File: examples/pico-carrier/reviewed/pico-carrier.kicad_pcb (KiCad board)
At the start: 2 copper layers, 88 x 62 mm, 16 parts, among them J1 5V IN, J3 GP0-GP15, J4 GP16-GP28, PWR, U1 Pico

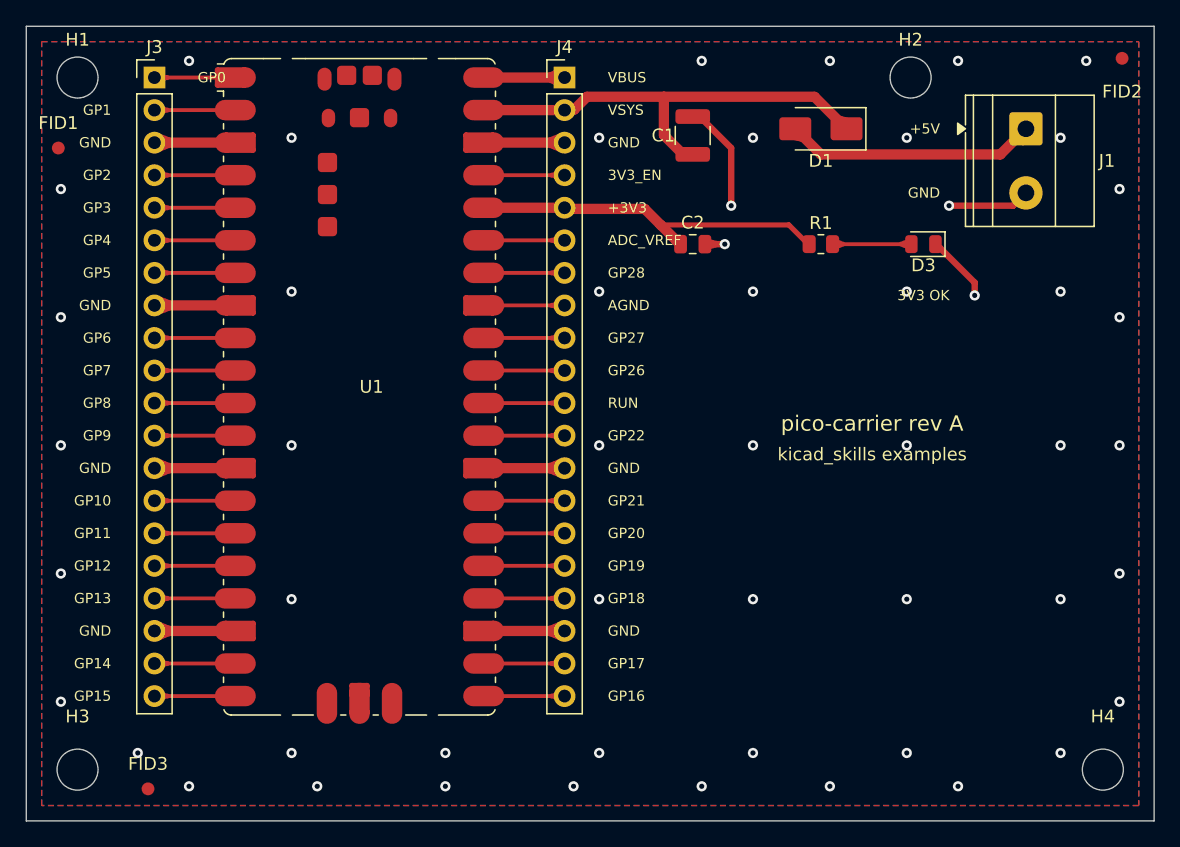
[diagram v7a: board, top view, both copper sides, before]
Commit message: Leave room for the screw, and print the ink where the board is
The screw holes were placed against the hole's own courtyard, which is the
drill plus a whisker - so on four of the five boards a hole sat inside a
connector's mating space, closest 0.42 mm. What goes through an M3 hole is a
pan head on a washer, seven millimetres of steel lying flat, and a connector
wants its shell, its wires and the fingers that fit them on top of that. The
spot search now keeps the fastener's own circle clear of every part body and
gives connectors CONNECTOR_ACCESS more, and three rules say so when a board
does not: mechanical.fastener_clearance, mechanical.connector_access and
mechanical.fastener_copper, all blocking for a generated design.

Silk was measured with a per-character advance of 0.78, and KiCad's stroke
font is proportional at 0.94 to 1.07. Everything downstream of that estimate
was placing ink where it did not fit: a legend across a capacitor's land, a
designator through the board's own name. `_text_extent` takes the top of the
measured range, adds the fab's clearance and is used by every silk placement.

Three placements also fell through to a position nobody chose. A designator
that found nothing kept its library offset, which for a part in a corner
points off the board; the board id took the first of eight fixed strips; a
legend took the least bad of six spots. All three are scored now, over
candidate sets wide enough to have an answer - and a pad-less footprint, which
is what a mounting hole is, is no longer skipped outright.

silk.off_board reports the case KiCad's own test cannot: ink that clears the
edge entirely is never printed, and DRC only measures ink that crosses it.

_unspiked redraws a corner tighter than a right angle as the elbow between its
neighbours - one diagonal, one straight, no step back to a heading the line
has already left. It is never longer than what it replaces.

All four fast boards: 0 errors, 0 warnings.

Co-Authored-By: Claude Fable 5 <no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
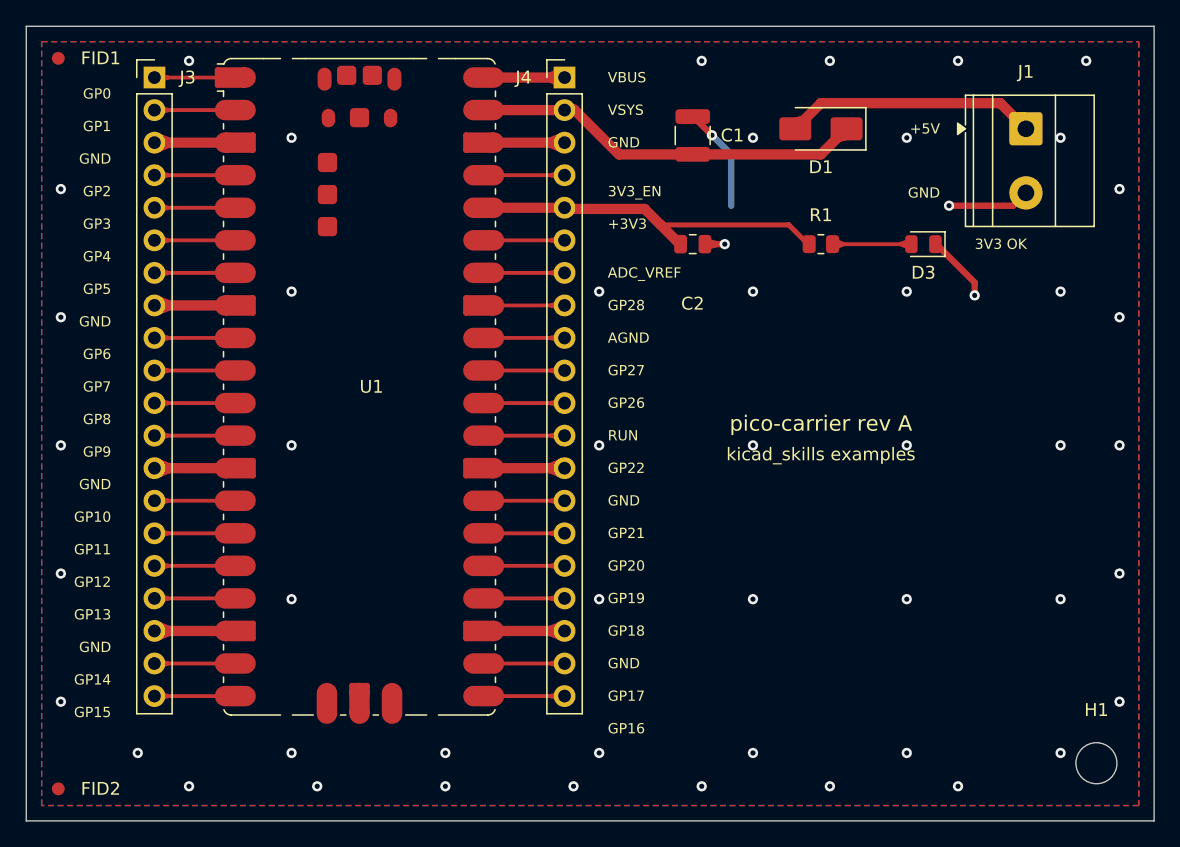
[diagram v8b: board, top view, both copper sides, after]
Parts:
- removed FID3: Fiducial, Fiducial:Fiducial_1mm_Mask2mm
- removed H2, H3, H4: M3, MountingHole:MountingHole_3.2mm_M3
- moved FID2 100.7 mm to (102.5, 119.5)
- moved H1 95.8 mm to (183.5, 117.5)
- moved FID1 7.00 mm to (102.5, 62.5)
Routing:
- net /VSYS: track 35.6 -> 30.6 mm
- net GND: track 66.0 -> 65.7 mm, vias 53 -> 52
